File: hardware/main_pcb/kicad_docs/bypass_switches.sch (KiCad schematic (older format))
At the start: 2 parts, among them U8 DG469EQ, U9 DG469EQ

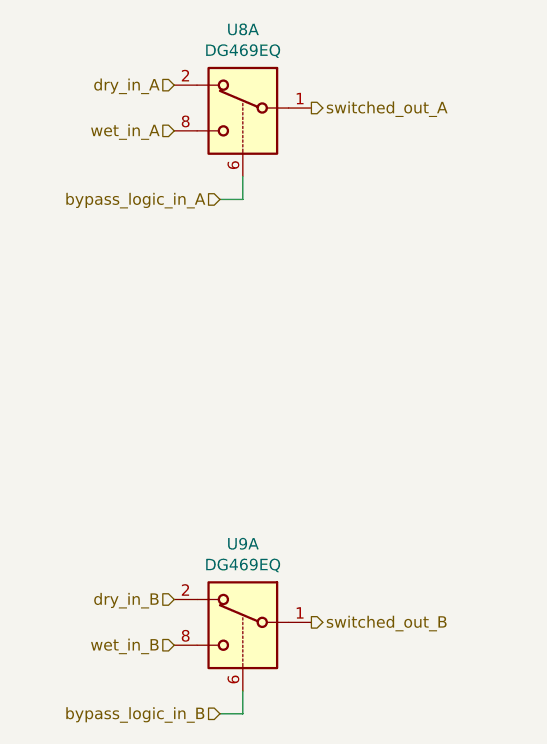
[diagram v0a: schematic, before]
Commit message: reduce analog switch count, tidy up
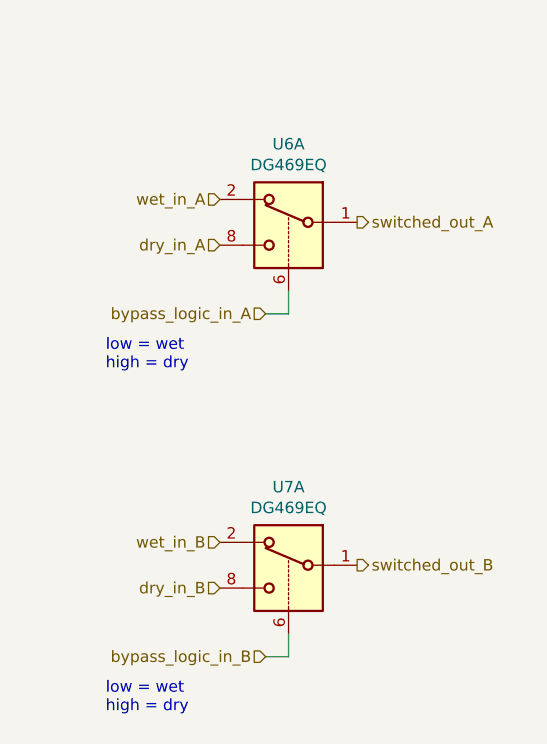
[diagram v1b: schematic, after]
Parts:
- renumbered U8 to U6, U9 to U7
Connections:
- net dry_in_A: now also U6.8; no longer U6.2
- net dry_in_B: now also U7.8; no longer U7.2
- net wet_in_A: now also U6.2; no longer U6.8
- net wet_in_B: now also U7.2; no longer U7.8
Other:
- note added: "low = wet\nhigh = dry"
- moved on the sheet: U6A, U7A
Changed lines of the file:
@@
 Comment4 ""
 $EndDescr
-Text HLabel 5300 2250 0    50   Input ~ 0
+Text HLabel 5500 2950 0    50   Input ~ 0
 dry_in_A
-Text HLabel 5300 2450 0    50   Input ~ 0
+Text HLabel 5500 2750 0    50   Input ~ 0
 wet_in_A
-Text HLabel 5300 4700 0    50   Input ~ 0
+Text HLabel 5500 4250 0    50   Input ~ 0
 wet_in_B
-Text HLabel 5300 4500 0    50   Input ~ 0
+Text HLabel 5500 4450 0    50   Input ~ 0
 dry_in_B
-Text HLabel 5900 2350 2    50   Output ~ 0
+Text HLabel 6100 2850 2    50   Output ~ 0
 switched_out_A
-Text HLabel 5900 4600 2    50   Output ~ 0
+Text HLabel 6100 4350 2    50   Output ~ 0
 switched_out_B
-Text HLabel 5500 2750 0    50   Input ~ 0
+Text HLabel 5700 3250 0    50   Input ~ 0
 bypass_logic_in_A
-Text HLabel 5500 5000 0    50   Input ~ 0
+Text HLabel 5700 4750 0    50   Input ~ 0
 bypass_logic_in_B
 Wire Wire Line
-	5500 2750 5600 2750
+	5700 3250 5800 3250
 Wire Wire Line
-	5600 2750 5600 2650
+	5800 3250 5800 3150
 Wire Wire Line
-	5500 5000 5600 5000
+	5700 4750 5800 4750
 Wire Wire Line
-	5600 5000 5600 4900
+	5800 4750 5800 4650
 $Comp
-L custom_components:DG469EQ U8
+L custom_components:DG469EQ U6
 U 1 1 6149CD4C
-P 5600 2250
-F 0 "U8" H 5600 2492 50  0000 C CNN
-F 1 "DG469EQ" H 5600 2401 50  0000 C CNN
-F 2 "Package_SO:MSOP-8_3x3mm_P0.65mm" H 5600 1950 50  0001 C CNN
-F 3 "https://datasheets.maximintegrated.com/en/ds/DG417-DG419.pdf" H 5600 2050 50  0001 C CNN
-	1    5600 2250
+P 5800 2750
+F 0 "U6" H 5800 2992 50  0000 C CNN
+F 1 "DG469EQ" H 5800 2901 50  0000 C CNN
+F 2 "Package_SO:MSOP-8_3x3mm_P0.65mm" H 5800 2450 50  0001 C CNN
+F 3 "https://datasheets.maximintegrated.com/en/ds/DG417-DG419.pdf" H 5800 2550 50  0001 C CNN
+	1    5800 2750
 	-1   0    0    -1
 $EndComp
 $Comp
-L custom_components:DG469EQ U9
+L custom_components:DG469EQ U7
 U 1 1 6149E09F
-P 5600 4500
-F 0 "U9" H 5600 4742 50  0000 C CNN
-F 1 "DG469EQ" H 5600 4651 50  0000 C CNN
-F 2 "Package_SO:MSOP-8_3x3mm_P0.65mm" H 5600 4200 50  0001 C CNN
-F 3 "https://datasheets.maximintegrated.com/en/ds/DG417-DG419.pdf" H 5600 4300 50  0001 C CNN
-	1    5600 4500
+P 5800 4250
+F 0 "U7" H 5800 4492 50  0000 C CNN
+F 1 "DG469EQ" H 5800 4401 50  0000 C CNN
+F 2 "Package_SO:MSOP-8_3x3mm_P0.65mm" H 5800 3950 50  0001 C CNN
+F 3 "https://datasheets.maximintegrated.com/en/ds/DG417-DG419.pdf" H 5800 4050 50  0001 C CNN
+	1    5800 4250
 	-1   0    0    -1
 $EndComp
+Text Notes 5000 3500 0    50   ~ 0
+low = wet\nhigh = dry
+Text Notes 5000 5000 0    50   ~ 0
+low = wet\nhigh = dry
 $EndSCHEMATC
